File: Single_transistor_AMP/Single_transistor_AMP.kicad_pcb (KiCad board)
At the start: 2 copper layers, 39.4 x 45.7 mm, 11 parts, among them P1 Input, P2 output, P3 power, Q1 BC548

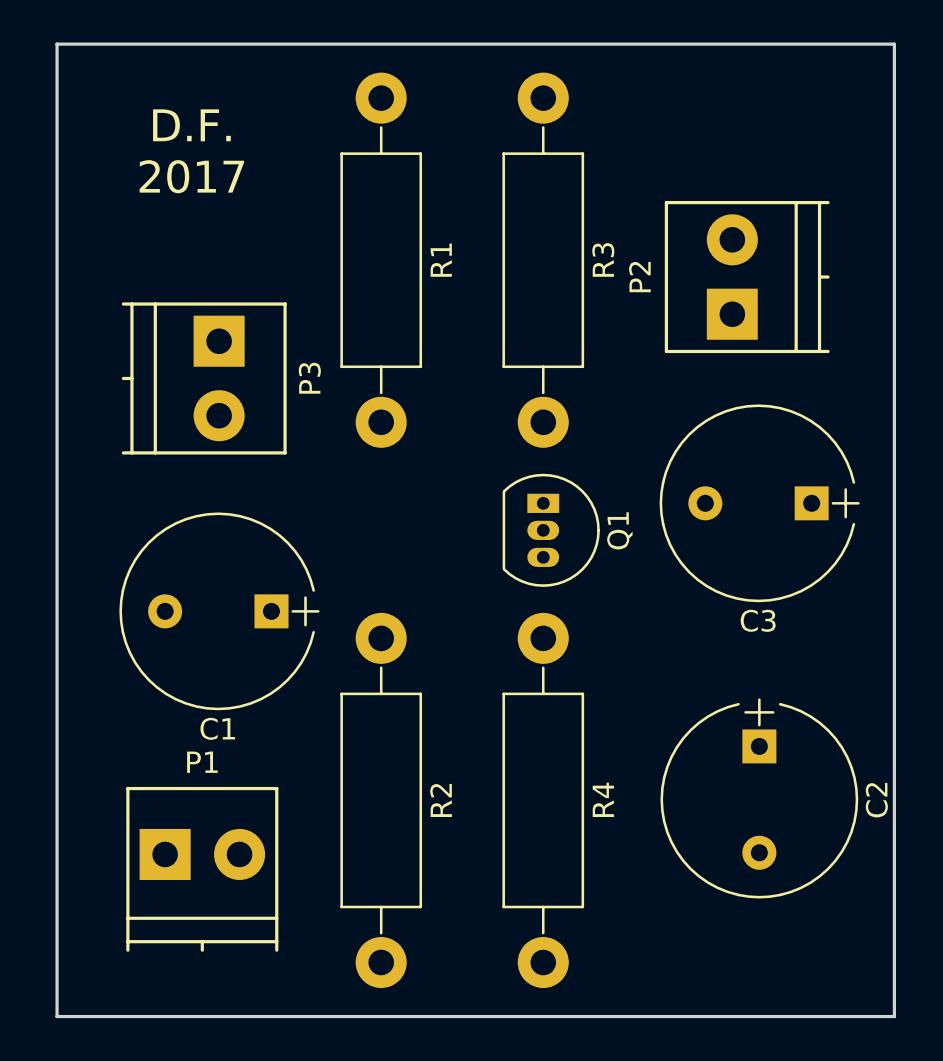
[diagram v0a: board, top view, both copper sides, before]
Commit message: Single transistor amp pabeigta plate
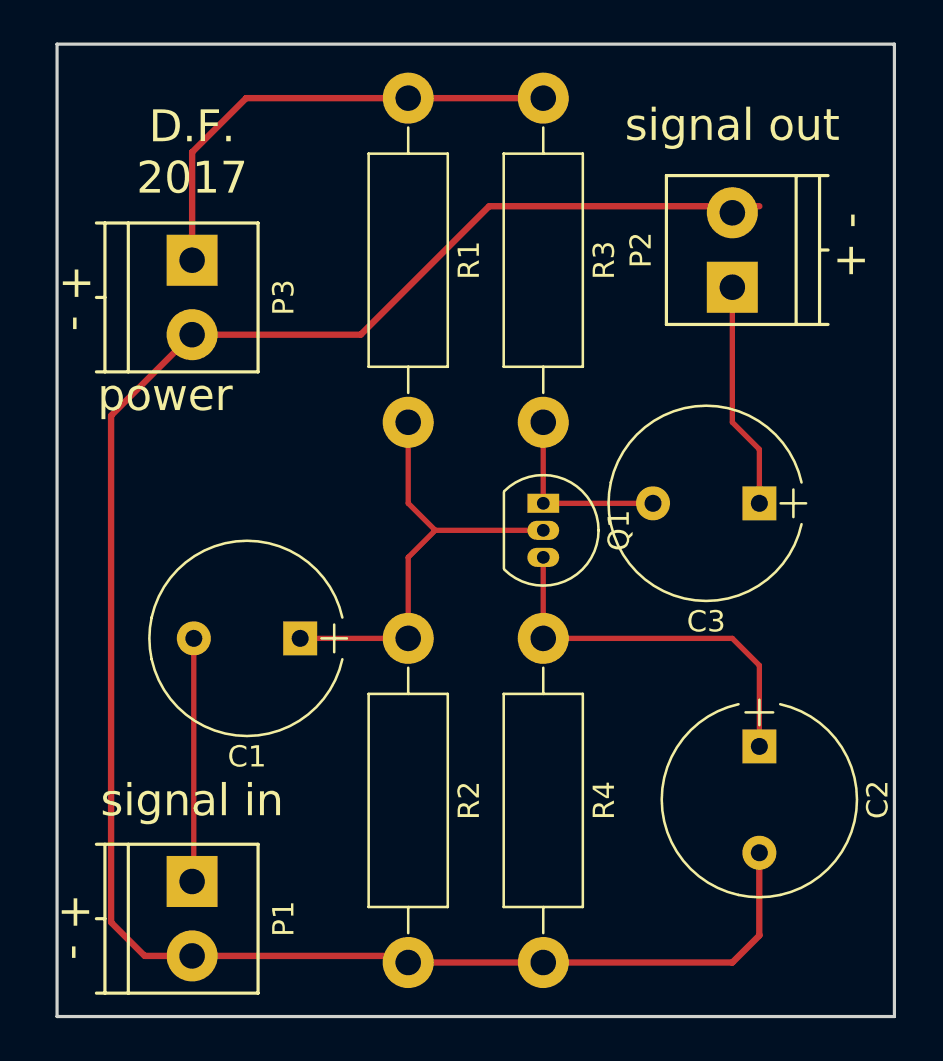
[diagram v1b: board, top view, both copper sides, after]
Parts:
- moved P3 4.02 mm to (69.8, 58.4)
- moved C3 2.46 mm to (96.5, 69.8)
- moved C1 1.85 mm to (74.9, 76.2)
- moved P1 1.80 mm to (69.8, 87.6), turned to 270 degrees
- moved R1 1.27 mm to (80.0, 50.8)
- moved R2 1.27 mm to (80.0, 76.2)
- moved P2 1.27 mm to (95.2, 59.7)
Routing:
- net GND: track 0.00 -> 94.1 mm
- net +12V: track 0.00 -> 22.6 mm
- net Net-(C1-Pad1): track 0.00 -> 21.4 mm
- net Net-(C2-Pad1): track 0.00 -> 18.3 mm
- net Net-(C1-Pad2): track 0.00 -> 11.5 mm
- net Net-(C3-Pad1): track 0.00 -> 10.7 mm
- net Net-(C3-Pad2): track 0.00 -> 8.97 mm
- added copper zone on F.Cu, net GND
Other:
- net class Power: trace_width 0.3 -> 1
- board text added: "+ -"
- board text added: "power"
- board text added: "signal in"
- board text added: "signal out"
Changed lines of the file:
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@@
   (general
     (links 16)
-    (no_connects 16)
-    (area 0 0 0 0)
+    (no_connects 0)
+    (area 63.424999 48.184999 102.945001 94.055001)
     (thickness 1.6)
-    (drawings 5)
-    (tracks 0)
+    (drawings 11)
+    (tracks 34)
     (zones 0)
     (modules 11)
@@
     (uvia_dia 0.3)
     (uvia_drill 0.1)
-    (add_net +12V)
-    (add_net GND)
     (add_net "Net-(C1-Pad1)")
     (add_net "Net-(C1-Pad2)")
@@
   (net_class Power ""
     (clearance 0.5)
-    (trace_width 0.3)
+    (trace_width 1)
     (via_dia 1)
     (via_drill 0.6)
     (uvia_dia 0.3)
     (uvia_drill 0.1)
+    (add_net +12V)
+    (add_net GND)
   )
   (module Capacitors_THT:CP_Radial_Tantal_D9.0mm_P5.00mm (layer F.Cu)
-    (at 73.58 74.93 180)
+    (at 74.93 76.2 180)
     (descr "CP, Radial_Tantal series, Radial, pin pitch=5.00mm, , diameter=9.0mm, Tantal Electrolytic Capacitor, http://cdn-reichelt.de/documents/datenblatt/B300/TANTAL-TB-Serie%23.pdf")
     (tags "CP Radial_Tantal series Radial pin pitch 5.00mm  diameter 9.0mm Tantal Electrolytic Capacitor")
@@
   )
   (module Capacitors_THT:CP_Radial_Tantal_D9.0mm_P5.00mm (layer F.Cu)
-    (at 98.98 69.85 180)
+    (at 96.52 69.85 180)
     (descr "CP, Radial_Tantal series, Radial, pin pitch=5.00mm, , diameter=9.0mm, Tantal Electrolytic Capacitor, http://cdn-reichelt.de/documents/datenblatt/B300/TANTAL-TB-Serie%23.pdf")
     (tags "CP Radial_Tantal series Radial pin pitch 5.00mm  diameter 9.0mm Tantal Electrolytic Capacitor")
@@
   )
   (module Connectors_Terminal_Blocks:TerminalBlock_Pheonix_PT-3.5mm_2pol (layer F.Cu)
-    (at 68.58 86.36)
+    (at 69.85 87.63 270)
     (descr "2-way 3.5mm pitch terminal block, Phoenix PT series")
-    (fp_text reference P1 (at 1.75 -4.3) (layer F.SilkS)
-      (effects (font (size 1 1) (thickness 0.15)))
-    )
-    (fp_text value Input (at 1.75 6) (layer F.Fab)
+    (fp_text reference P1 (at 1.75 -4.3 270) (layer F.SilkS)
+      (effects (font (size 1 1) (thickness 0.15)))
+    )
+    (fp_text value Input (at 1.75 6 270) (layer F.Fab)
       (effects (font (size 1 1) (thickness 0.15)))
     )
@@
     (fp_line (start 5.25 4.5) (end 5.25 -3.1) (layer F.SilkS) (width 0.15))
     (fp_line (start 5.25 -3.1) (end -1.75 -3.1) (layer F.SilkS) (width 0.15))
-    (pad 2 thru_hole circle (at 3.5 0) (size 2.4 2.4) (drill 1.2) (layers *.Cu *.Mask)
+    (pad 2 thru_hole circle (at 3.5 0 270) (size 2.4 2.4) (drill 1.2) (layers *.Cu *.Mask)
       (net 4 GND))
-    (pad 1 thru_hole rect (at 0 0) (size 2.4 2.4) (drill 1.2) (layers *.Cu *.Mask)
+    (pad 1 thru_hole rect (at 0 0 270) (size 2.4 2.4) (drill 1.2) (layers *.Cu *.Mask)
       (net 2 "Net-(C1-Pad2)"))
     (model Terminal_Blocks.3dshapes/TerminalBlock_Pheonix_PT-3.5mm_2pol.wrl
@@
   )
   (module Connectors_Terminal_Blocks:TerminalBlock_Pheonix_PT-3.5mm_2pol (layer F.Cu)
-    (at 95.25 60.96 90)
+    (at 95.25 59.69 90)
     (descr "2-way 3.5mm pitch terminal block, Phoenix PT series")
     (fp_text reference P2 (at 1.75 -4.3 90) (layer F.SilkS)
@@
   )
   (module Connectors_Terminal_Blocks:TerminalBlock_Pheonix_PT-3.5mm_2pol (layer F.Cu)
-    (at 71.12 62.23 270)
+    (at 69.85 58.42 270)
     (descr "2-way 3.5mm pitch terminal block, Phoenix PT series")
     (fp_text reference P3 (at 1.75 -4.3 270) (layer F.SilkS)
@@
   )
   (module Resistors_THT:R_Axial_DIN0411_L9.9mm_D3.6mm_P15.24mm_Horizontal (layer F.Cu)
-    (at 78.74 50.8 270)
+    (at 80.01 50.8 270)
     (descr "Resistor, Axial_DIN0411 series, Axial, Horizontal, pin pitch=15.24mm, 1W = 1/1W, length*diameter=9.9*3.6mm^2")
     (tags "Resistor Axial_DIN0411 series Axial Horizontal pin pitch 15.24mm 1W = 1/1W length 9.9mm diameter 3.6mm")
@@
   )
   (module Resistors_THT:R_Axial_DIN0411_L9.9mm_D3.6mm_P15.24mm_Horizontal (layer F.Cu)
-    (at 78.74 76.2 270)
+    (at 80.01 76.2 270)
     (descr "Resistor, Axial_DIN0411 series, Axial, Horizontal, pin pitch=15.24mm, 1W = 1/1W, length*diameter=9.9*3.6mm^2")
     (tags "Resistor Axial_DIN0411 series Axial Horizontal pin pitch 15.24mm 1W = 1/1W length 9.9mm diameter 3.6mm")
@@
     )
   )
+  (gr_text "+ -" (at 100.7872 57.7342 90) (layer F.SilkS)
+    (effects (font (size 1.5 1.5) (thickness 0.3)))
+  )
+  (gr_text "+ -" (at 64.4144 89.7636 270) (layer F.SilkS)
+    (effects (font (size 1.5 1.5) (thickness 0.3)))
+  )
+  (gr_text "+ -" (at 64.4652 60.198 270) (layer F.SilkS)
+    (effects (font (size 1.5 1.5) (thickness 0.3)))
+  )
+  (gr_text "signal out" (at 95.25 52.07) (layer F.SilkS)
+    (effects (font (size 1.5 1.5) (thickness 0.3)))
+  )
+  (gr_text power (at 68.58 64.77) (layer F.SilkS)
+    (effects (font (size 1.5 1.5) (thickness 0.3)))
+  )
+  (gr_text "signal in" (at 69.85 83.82) (layer F.SilkS)
+    (effects (font (size 1.5 1.5) (thickness 0.3)))
+  )
   (gr_text "D.F.\n2017" (at 69.85 53.34) (layer F.SilkS)
     (effects (font (size 1.5 1.5) (thickness 0.3)))
@@
   (gr_line (start 102.87 48.26) (end 102.87 93.98) (layer Edge.Cuts) (width 0.15))
   (gr_line (start 63.5 48.26) (end 102.87 48.26) (layer Edge.Cuts) (width 0.15))
+  (segment (start 81.28 71.12) (end 86.36 71.12) (width 0.25) (layer F.Cu) (net 1))
+  (segment (start 80.01 69.85) (end 81.28 71.12) (width 0.25) (layer F.Cu) (net 1))
+  (segment (start 80.01 66.04) (end 80.01 69.85) (width 0.25) (layer F.Cu) (net 1))
+  (segment (start 80.01 72.39) (end 81.28 71.12) (width 0.25) (layer F.Cu) (net 1))
+  (segment (start 80.01 76.2) (end 80.01 72.39) (width 0.25) (layer F.Cu) (net 1))
+  (segment (start 74.93 76.2) (end 80.01 76.2) (width 0.25) (layer F.Cu) (net 1))
+  (segment (start 69.93 76.2) (end 69.93 87.55) (width 0.25) (layer F.Cu) (net 2))
+  (segment (start 69.93 87.55) (end 69.85 87.63) (width 0.25) (layer F.Cu) (net 2))
+  (segment (start 95.25 76.2) (end 86.36 76.2) (width 0.25) (layer F.Cu) (net 3))
+  (segment (start 96.52 77.47) (end 95.25 76.2) (width 0.25) (layer F.Cu) (net 3))
+  (segment (start 96.52 81.28) (end 96.52 77.47) (width 0.25) (layer F.Cu) (net 3))
+  (segment (start 86.36 72.39) (end 86.36 76.2) (width 0.25) (layer F.Cu) (net 3))
+  (segment (start 83.82 55.88) (end 77.78 61.92) (width 0.3) (layer F.Cu) (net 4))
+  (segment (start 77.78 61.92) (end 69.85 61.92) (width 0.3) (layer F.Cu) (net 4))
+  (segment (start 96.52 55.88) (end 83.82 55.88) (width 0.3) (layer F.Cu) (net 4))
+  (segment (start 69.85 91.13) (end 67.62 91.13) (width 0.3) (layer F.Cu) (net 4))
+  (segment (start 67.62 91.13) (end 66.04 89.55) (width 0.3) (layer F.Cu) (net 4))
+  (segment (start 66.04 89.55) (end 66.04 65.73) (width 0.3) (layer F.Cu) (net 4))
+  (segment (start 66.04 65.73) (end 69.85 61.92) (width 0.3) (layer F.Cu) (net 4))
+  (segment (start 95.25 91.44) (end 86.36 91.44) (width 0.3) (layer F.Cu) (net 4))
+  (segment (start 96.52 90.17) (end 95.25 91.44) (width 0.3) (layer F.Cu) (net 4))
+  (segment (start 96.52 86.28) (end 96.52 90.17) (width 0.3) (layer F.Cu) (net 4))
+  (segment (start 80.01 91.44) (end 86.36 91.44) (width 0.3) (layer F.Cu) (net 4))
+  (segment (start 69.85 91.13) (end 79.7 91.13) (width 0.3) (layer F.Cu) (net 4))
+  (segment (start 79.7 91.13) (end 80.01 91.44) (width 0.3) (layer F.Cu) (net 4))
+  (segment (start 95.25 66.04) (end 96.52 67.31) (width 0.25) (layer F.Cu) (net 5))
+  (segment (start 96.52 67.31) (end 96.52 69.85) (width 0.25) (layer F.Cu) (net 5))
+  (segment (start 95.25 59.69) (end 95.25 66.04) (width 0.25) (layer F.Cu) (net 5))
+  (segment (start 86.36 69.85) (end 91.52 69.85) (width 0.25) (layer F.Cu) (net 6))
+  (segment (start 86.36 69.85) (end 86.36 66.04) (width 0.25) (layer F.Cu) (net 6))
+  (segment (start 80.01 50.8) (end 86.36 50.8) (width 0.3) (layer F.Cu) (net 7))
+  (segment (start 69.85 58.42) (end 69.85 53.34) (width 0.3) (layer F.Cu) (net 7))
+  (segment (start 69.85 53.34) (end 72.39 50.8) (width 0.3) (layer F.Cu) (net 7))
+  (segment (start 72.39 50.8) (end 80.01 50.8) (width 0.3) (layer F.Cu) (net 7))
+  (zone (net 4) (net_name GND) (layer F.Cu) (hatch edge 0.508)
+    (connect_pads (clearance 0.508))
+    (min_thickness 0.254)
+    (fill yes (arc_segments 16) (thermal_gap 0.508) (thermal_bridge_width 0.508))
+    (polygon
+      (pts
+        (xy 63.5 48.26) (xy 63.5 93.98) (xy 102.87 93.98) (xy 102.87 48.26)
+      )
+    )
+  )
 )
